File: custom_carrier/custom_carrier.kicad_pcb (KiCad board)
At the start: 4 copper layers, 70 x 75 mm, 16 parts, among them J1 ERF5-040-05.0-X-DV, J13 PJ-002AH-SMT-TR, J14 87832-1420, J2 ERF5-040-05.0-X-DV, J3 ERF5-040-05.0-X-DV, J4 ERF5-040-05.0-X-DV, J5 45230-220230, J6 45230-220230

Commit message: slight cleanup
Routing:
- net GND: track 212.4 -> 200.1 mm, vias 137 -> 133
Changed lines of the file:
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@@
     (property "Sheetname" "")
     (attr smd)
-    (fp_text reference "J13" (at -8.0628 -2.81774) (layer "F.SilkS")
+    (fp_text reference "J13" (at -9.57 -0.932) (layer "F.SilkS")
         (effects (font (size 1.000976 1.000976) (thickness 0.15)))
     )
@@
         (effects (font (size 1.000677 1.000677) (thickness 0.15)))
     )
-    (fp_text value "87832-1420" (at 6.36354 9.520345 90) (layer "F.Fab")
+    (fp_text value "87832-1420" (at -1.11065 -0.31 180) (layer "F.Fab")
         (effects (font (size 1.000559 1.000559) (thickness 0.15)))
     )
@@
     (property "partnumber" "TCJB226M025R0150")
     (attr smd)
-    (fp_text reference "C1" (at -4.3315 0 -270) (layer "F.SilkS")
+    (fp_text reference "C1" (at -0.086 -2.584 -270) (layer "F.SilkS")
         (effects (font (size 1 1) (thickness 0.15)))
     )
@@
   (gr_rect (start 95 75) (end 165 150)
     (stroke (width 0.05) (type default)) (fill none) (layer "Edge.Cuts"))
-  (segment (start 145.4531 127.439612) (end 145.4531 132.773612) (width 0.2032) (layer "F.Cu") (net 1))
-  (segment (start 146.8501 134.170612) (end 146.8501 141.135099) (width 0.2032) (layer "F.Cu") (net 1))
-  (segment (start 145.4531 132.773612) (end 146.8501 134.170612) (width 0.2032) (layer "F.Cu") (net 1))
-  (segment (start 139.25 120.100001) (end 139.1651 120.184901) (width 0.2032) (layer "F.Cu") (net 1))
-  (segment (start 146.8501 141.135099) (end 147.32 141.604999) (width 0.2032) (layer "F.Cu") (net 1))
-  (segment (start 139.25 118.975) (end 139.25 120.100001) (width 0.2032) (layer "F.Cu") (net 1))
-  (segment (start 147.32 141.604999) (end 147.32 143.51) (width 0.2032) (layer "F.Cu") (net 1))
-  (segment (start 139.1651 120.184901) (end 139.1651 121.151612) (width 0.2032) (layer "F.Cu") (net 1))
-  (segment (start 139.1651 121.151612) (end 145.4531 127.439612) (width 0.2032) (layer "F.Cu") (net 1))
-  (segment (start 145.1229 132.910388) (end 146.5199 134.307388) (width 0.2032) (layer "F.Cu") (net 7))
-  (segment (start 145.1229 127.576388) (end 145.1229 132.910388) (width 0.2032) (layer "F.Cu") (net 7))
-  (segment (start 146.5199 134.307388) (end 146.5199 141.135099) (width 0.2032) (layer "F.Cu") (net 7))
-  (segment (start 138.8349 120.184901) (end 138.8349 121.288388) (width 0.2032) (layer "F.Cu") (net 7))
-  (segment (start 138.75 118.975) (end 138.75 120.100001) (width 0.2032) (layer "F.Cu") (net 7))
-  (segment (start 146.05 141.604999) (end 146.05 143.51) (width 0.2032) (layer "F.Cu") (net 7))
-  (segment (start 138.75 120.100001) (end 138.8349 120.184901) (width 0.2032) (layer "F.Cu") (net 7))
-  (segment (start 146.5199 141.135099) (end 146.05 141.604999) (width 0.2032) (layer "F.Cu") (net 7))
-  (segment (start 138.8349 121.288388) (end 145.1229 127.576388) (width 0.2032) (layer "F.Cu") (net 7))
+  (segment (start 139.25 120.100001) (end 139.25 118.975) (width 0.2032) (layer "F.Cu") (net 1))
+  (segment (start 147.32 143.51) (end 147.32 141.604999) (width 0.2032) (layer "F.Cu") (net 1))
+  (segment (start 139.1651 121.151612) (end 139.1651 120.184901) (width 0.2032) (layer "F.Cu") (net 1))
+  (segment (start 146.8501 128.836612) (end 139.1651 121.151612) (width 0.2032) (layer "F.Cu") (net 1))
+  (segment (start 139.1651 120.184901) (end 139.25 120.100001) (width 0.2032) (layer "F.Cu") (net 1))
+  (segment (start 147.32 141.604999) (end 146.8501 141.135099) (width 0.2032) (layer "F.Cu") (net 1))
+  (segment (start 146.8501 141.135099) (end 146.8501 128.836612) (width 0.2032) (layer "F.Cu") (net 1))
+  (segment (start 146.05 143.51) (end 146.05 141.604999) (width 0.2032) (layer "F.Cu") (net 7))
+  (segment (start 138.8349 121.288388) (end 138.8349 120.184901) (width 0.2032) (layer "F.Cu") (net 7))
+  (segment (start 138.75 120.100001) (end 138.75 118.975) (width 0.2032) (layer "F.Cu") (net 7))
+  (segment (start 138.8349 120.184901) (end 138.75 120.100001) (width 0.2032) (layer "F.Cu") (net 7))
+  (segment (start 146.05 141.604999) (end 146.5199 141.135099) (width 0.2032) (layer "F.Cu") (net 7))
+  (segment (start 146.5199 128.973388) (end 138.8349 121.288388) (width 0.2032) (layer "F.Cu") (net 7))
+  (segment (start 146.5199 141.135099) (end 146.5199 128.973388) (width 0.2032) (layer "F.Cu") (net 7))
   (segment (start 144.3101 128.328612) (end 144.3101 141.135099) (width 0.2032) (layer "F.Cu") (net 13))
   (segment (start 144.3101 141.135099) (end 144.78 141.604999) (width 0.2032) (layer "F.Cu") (net 13))
@@
   (segment (start 153.67 147.574) (end 153.67 145.52) (width 0.254) (layer "F.Cu") (net 211))
   (segment (start 139.773772 115.001228) (end 139.75 115.025) (width 0.254) (layer "F.Cu") (net 211))
-  (segment (start 103 83) (end 106.35 83) (width 0.254) (layer "F.Cu") (net 211))
   (segment (start 133.713443 113.744303) (end 133.713443 114.988443) (width 0.254) (layer "F.Cu") (net 211))
   (segment (start 160.25 90.22) (end 159.005 90.22) (width 0.19558) (layer "F.Cu") (net 211))
   (segment (start 123.27 81.005) (end 123.25 81.025) (width 0.19558) (layer "F.Cu") (net 211))
-  (segment (start 157 117) (end 155.06 118.94) (width 0.254) (layer "F.Cu") (net 211))
   (segment (start 127.756025 113.744303) (end 127.756025 115.018975) (width 0.254) (layer "F.Cu") (net 211))
-  (segment (start 157 83) (end 153.69 83) (width 0.254) (layer "F.Cu") (net 211))
   (segment (start 158.995 109.77) (end 158.975 109.75) (width 0.19558) (layer "F.Cu") (net 211))
   (segment (start 160.27 92.8) (end 159.025 92.8) (width 0.19558) (layer "F.Cu") (net 211))
@@
   (segment (start 160.28 105.22) (end 159.005 105.22) (width 0.19558) (layer "F.Cu") (net 211))
   (segment (start 126.238 141.642) (end 126.29 141.59) (width 0.19558) (layer "F.Cu") (net 211))
-  (segment (start 155.06 118.94) (end 154.69 118.94) (width 0.254) (layer "F.Cu") (net 211))
   (segment (start 106.23 106.75) (end 106.25 106.77) (width 0.254) (layer "F.Cu") (net 211))
   (segment (start 106.17 97.75) (end 106.18 97.76) (width 0.254) (layer "F.Cu") (net 211))
@@
   (segment (start 136.743607 113.744303) (end 136.743607 115.018607) (width 0.254) (layer "F.Cu") (net 211))
   (segment (start 158.21 133.80935) (end 158.21 136.03) (width 0.254) (layer "F.Cu") (net 211))
-  (segment (start 153.69 83) (end 153.68 83.01) (width 0.254) (layer "F.Cu") (net 211))
   (segment (start 129.253955 113.744303) (end 129.253955 115.021045) (width 0.254) (layer "F.Cu") (net 211))
   (segment (start 106.2 137.95) (end 106.17 137.98) (width 0.19558) (layer "F.Cu") (net 211))
   (segment (start 142.24 149.3) (end 142.26 149.32) (width 0.254) (layer "F.Cu") (net 211))
   (segment (start 119.888 149.368) (end 119.89 149.37) (width 0.254) (layer "F.Cu") (net 211))
-  (segment (start 103.32 117) (end 105.05 118.73) (width 0.254) (layer "F.Cu") (net 211))
   (segment (start 148.59 145.56) (end 148.57 145.54) (width 0.254) (layer "F.Cu") (net 211))
   (segment (start 124.794468 114.980532) (end 124.75 115.025) (width 0.254) (layer "F.Cu") (net 211))
@@
   (segment (start 126.26 81.015) (end 126.25 81.025) (width 0.19558) (layer "F.Cu") (net 211))
   (segment (start 156.21 136) (end 156.31 136.1) (width 0.254) (layer "F.Cu") (net 211))
-  (segment (start 106.35 83) (end 106.36 83.01) (width 0.254) (layer "F.Cu") (net 211))
   (segment (start 130.740451 113.755738) (end 130.740451 115.015451) (width 0.254) (layer "F.Cu") (net 211))
   (segment (start 128.75 86.23) (end 128.75 84.975) (width 0.19558) (layer "F.Cu") (net 211))
@@
   (via (at 126.28 86.22) (size 0.508) (drill 0.254) (layers "F.Cu" "B.Cu") (free) (net 211))
   (via (at 99.71 102.25) (size 0.508) (drill 0.254) (layers "F.Cu" "B.Cu") (free) (net 211))
-  (via (at 106.36 83.01) (size 0.508) (drill 0.254) (layers "F.Cu" "B.Cu") (net 211))
   (via (at 129.253504 113.58) (size 0.508) (drill 0.254) (layers "F.Cu" "B.Cu") (free) (net 211))
   (via (at 132.203627 113.58) (size 0.508) (drill 0.254) (layers "F.Cu" "B.Cu") (free) (net 211))
@@
   (via (at 158.2 136.04) (size 0.508) (drill 0.254) (layers "F.Cu" "B.Cu") (net 211))
   (via (at 99.68 89.64) (size 0.508) (drill 0.254) (layers "F.Cu" "B.Cu") (free) (net 211))
-  (via (at 153.68 83.01) (size 0.508) (drill 0.254) (layers "F.Cu" "B.Cu") (net 211))
   (via (at 136.26 79.76) (size 0.508) (drill 0.254) (layers "F.Cu" "B.Cu") (free) (net 211))
   (via (at 139.773321 113.58) (size 0.508) (drill 0.254) (layers "F.Cu" "B.Cu") (free) (net 211))
@@
   (via (at 130.74 113.58) (size 0.508) (drill 0.254) (layers "F.Cu" "B.Cu") (free) (net 211))
   (via (at 131.24 86.23) (size 0.508) (drill 0.254) (layers "F.Cu" "B.Cu") (free) (net 211))
-  (via (at 154.69 118.94) (size 0.508) (drill 0.254) (layers "F.Cu" "B.Cu") (net 211))
   (via (at 118.62 145.55) (size 0.508) (drill 0.254) (layers "F.Cu" "B.Cu") (net 211))
   (via (at 121.749549 120.38) (size 0.508) (drill 0.254) (layers "F.Cu" "B.Cu") (free) (net 211))
@@
   (via (at 160.26 97.79) (size 0.508) (drill 0.254) (layers "F.Cu" "B.Cu") (free) (net 211))
   (via (at 121.729549 113.58) (size 0.508) (drill 0.254) (layers "F.Cu" "B.Cu") (free) (net 211))
-  (via (at 105.05 118.73) (size 0.508) (drill 0.254) (layers "F.Cu" "B.Cu") (net 211))
   (via (at 153.74 109.75) (size 0.508) (drill 0.254) (layers "F.Cu" "B.Cu") (free) (net 211))
   (via (at 141.949549 113.58) (size 0.508) (drill 0.254) (layers "F.Cu" "B.Cu") (free) (net 211))

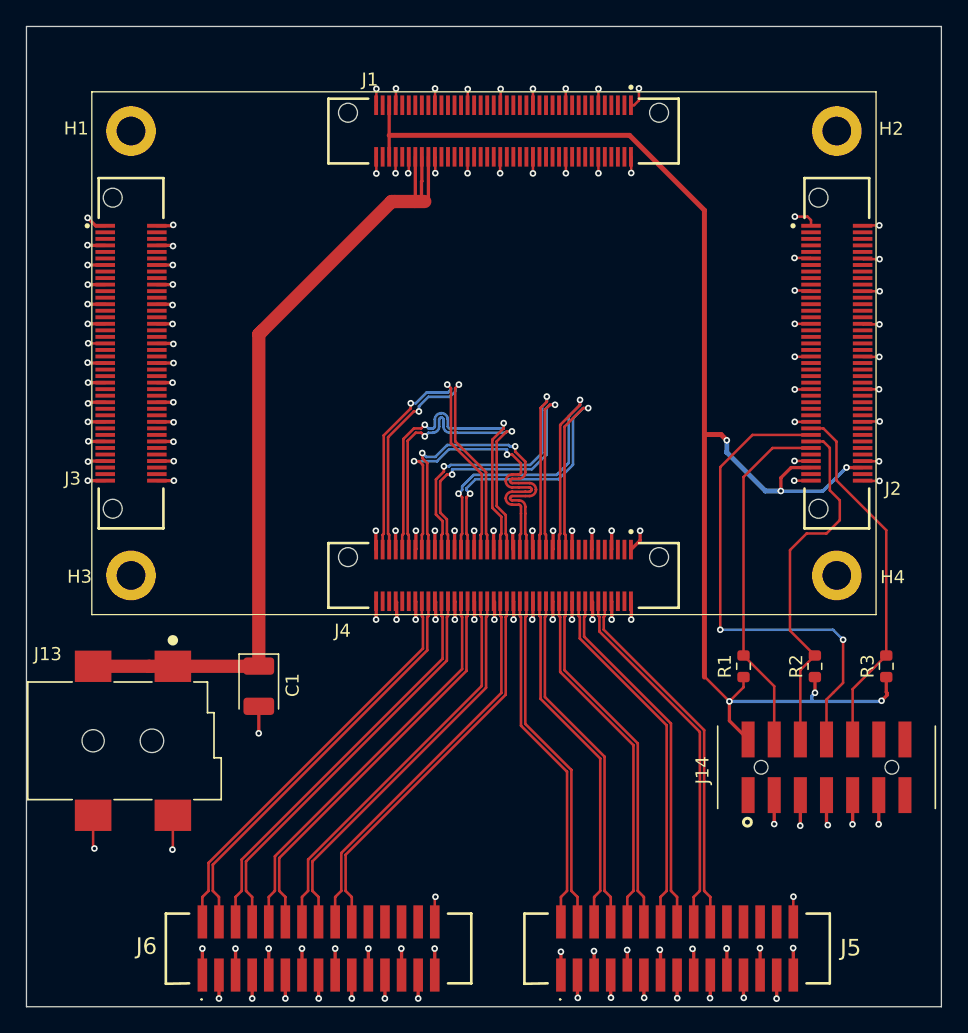
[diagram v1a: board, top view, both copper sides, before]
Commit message: rewired 3M connectors to recommended diff pair arrangement. tuned diff pair skews.
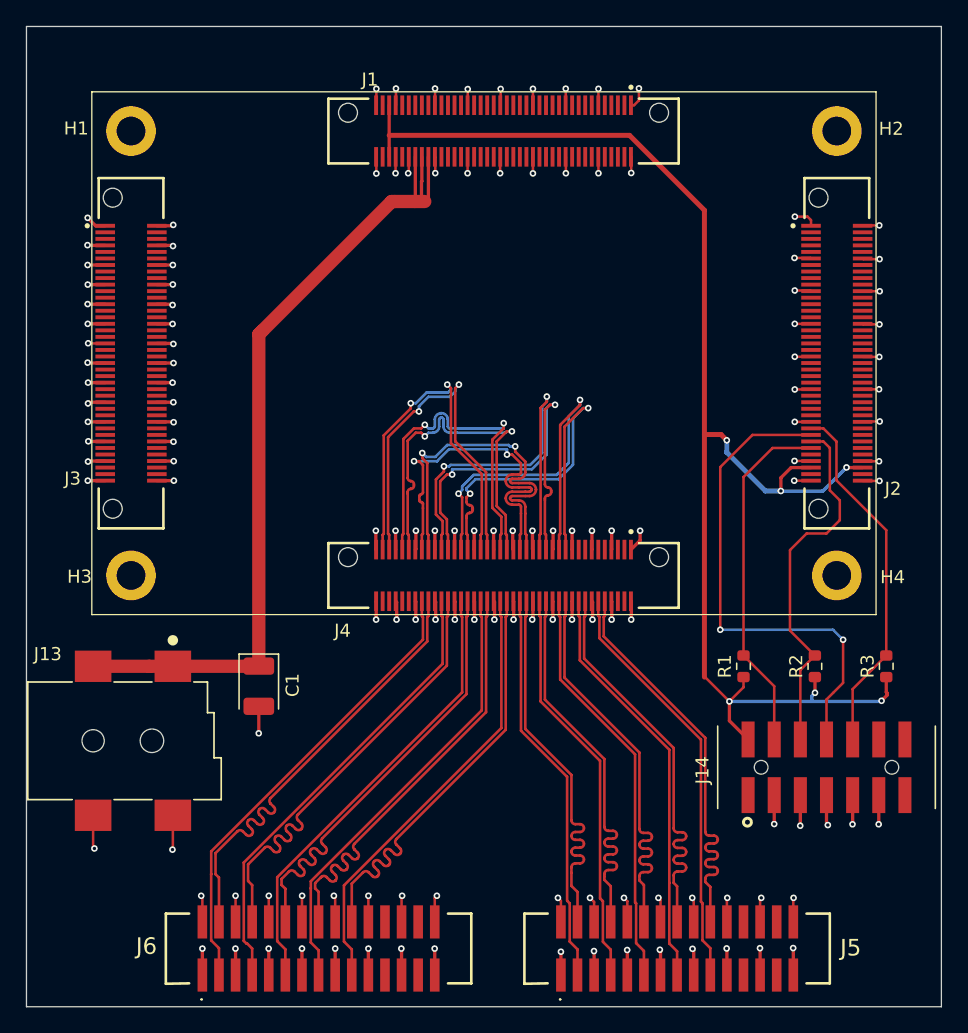
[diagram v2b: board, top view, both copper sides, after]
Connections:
- J5 pad 10: /CH1_RX1_N -> GND
- J5 pad 11: GND -> /CH1_RX1_N
- J5 pad 14: /CH1_RX2_N -> GND
- J5 pad 15: GND -> /CH1_RX2_N
- J5 pad 18: /CH1_RX3_N -> GND
- J5 pad 19: GND -> /CH1_RX3_N
- J5 pad 2: /CH1_DCO_N -> GND
- J5 pad 22: unconnected-(J5-Pad22) -> GND
- J5 pad 23: GND -> unconnected-(J5-Pad23)
- J5 pad 26: unconnected-(J5-Pad26) -> GND
- J5 pad 27: GND -> unconnected-(J5-Pad27)
- J5 pad 3: GND -> /CH1_DCO_N
- J5 pad 6: /CH1_RX0_N -> GND
- J5 pad 7: GND -> /CH1_RX0_N
- J6 pad 10: /CH1_TX1_N -> GND
- J6 pad 11: GND -> /CH1_TX1_N
- J6 pad 14: /CH1_TX2_N -> GND
- J6 pad 15: GND -> /CH1_TX2_N
- J6 pad 18: /CH1_TX3_N -> GND
- J6 pad 19: GND -> /CH1_TX3_N
- J6 pad 2: /CH1_CLK_N -> GND
- J6 pad 22: unconnected-(J6-Pad22) -> GND
- J6 pad 23: GND -> unconnected-(J6-Pad23)
- J6 pad 26: unconnected-(J6-Pad26) -> GND
- J6 pad 27: GND -> unconnected-(J6-Pad27)
- J6 pad 3: GND -> /CH1_CLK_N
- J6 pad 6: /CH1_TX0_N -> GND
- J6 pad 7: GND -> /CH1_TX0_N
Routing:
- net /CH1_RX2_N: track 27.5 -> 31.7 mm
- net /CH1_RX1_N: track 27.1 -> 31.3 mm
- net /CH1_RX0_N: track 26.7 -> 30.9 mm
- net /CH1_RX3_N: track 27.9 -> 32.1 mm
- net /CH1_DCO_N: track 26.2 -> 30.4 mm
- net /CH1_TX0_N: track 31.1 -> 35.2 mm
- net /CH1_RX2_P: track 27.5 -> 31.6 mm
- net /CH1_RX3_P: track 27.9 -> 32.0 mm
- net /CH1_RX0_P: track 26.7 -> 30.7 mm
- net /CH1_RX1_P: track 27.1 -> 31.1 mm
- net /CH1_DCO_P: track 26.2 -> 30.3 mm
- net /CH1_TX1_N: track 30.7 -> 34.8 mm
- net /CH1_TX3_N: track 29.8 -> 33.9 mm
- net /CH1_TX2_N: track 30.3 -> 34.3 mm
- net /CH1_CLK_N: track 31.6 -> 35.6 mm
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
